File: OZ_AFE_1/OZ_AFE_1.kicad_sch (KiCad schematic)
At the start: 58 parts, among them U1 LT6011, U2 TLV2211, U3 ISL21009BFB825Z, U4 LT6011, U5 OGS, U6 MCP9700x-HTT

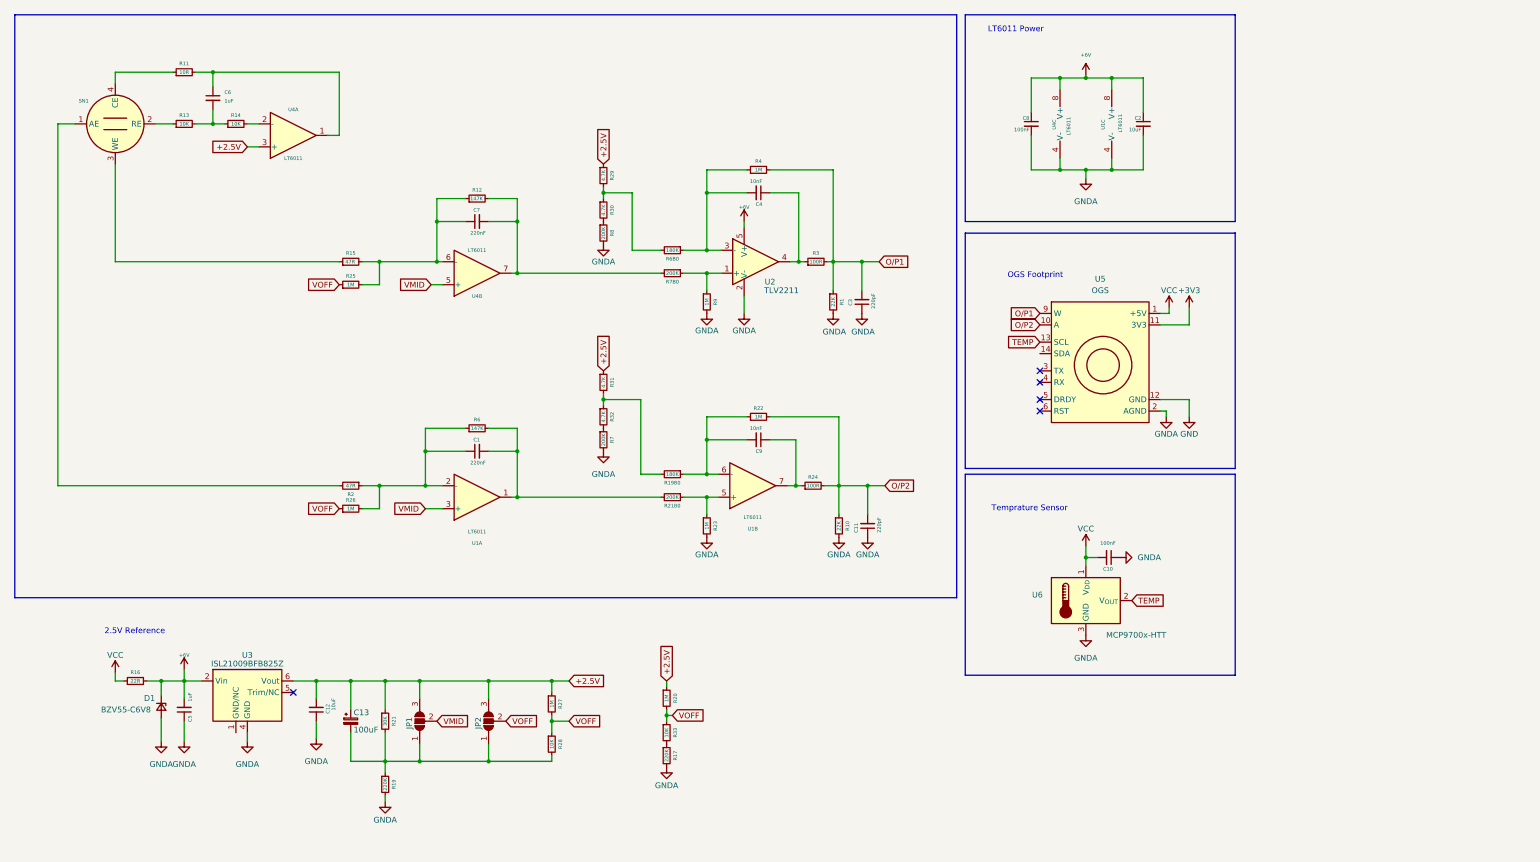
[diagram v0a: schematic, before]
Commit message: New Simulation and PCB
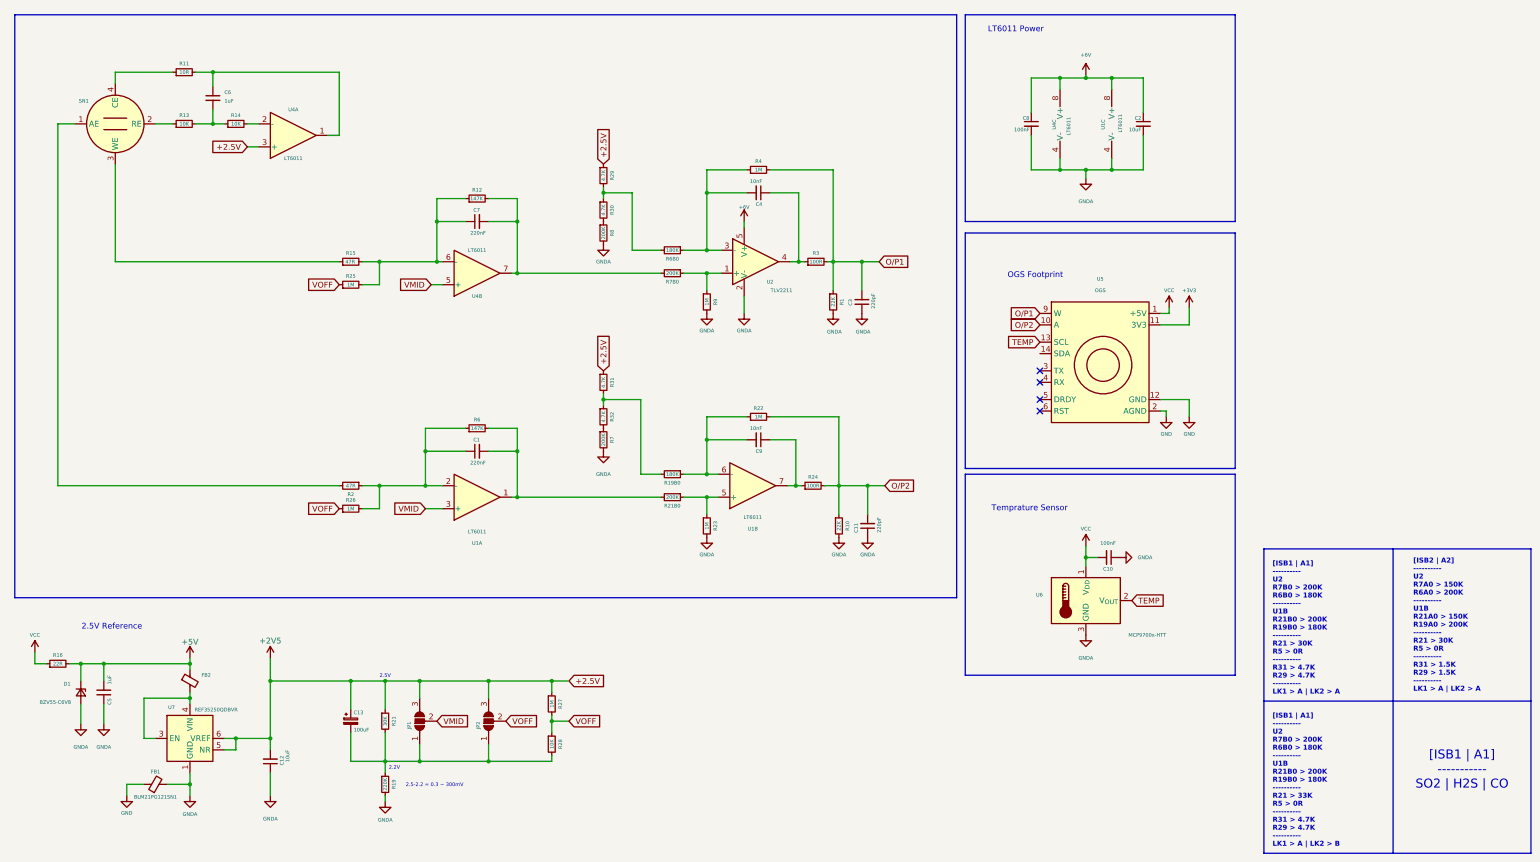
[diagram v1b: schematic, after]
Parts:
- removed R17: 220K, Resistor_SMD:R_0603_1608Metric, symbol Device:R_Small
- removed R20: 1M, Resistor_SMD:R_0603_1608Metric, symbol Device:R_Small
- removed R33: 10K, Resistor_SMD:R_0603_1608Metric, symbol Device:R_Small
- removed U3: ISL21009BFB825Z, Package_SO:SOIC-8_3.9x4.9mm_P1.27mm, symbol Voltage-Reference:ISL21009BFB825Z
- added FB1, FB2: BLM21PG121SN1, symbol Device:FerriteBead_Small
- added U7: REF35250QDBVR, Package_TO_SOT_SMD:SOT-23-6, symbol Reference_Voltage:REF35250QDBVR
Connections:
- net +6V: no longer C5.2, D1.1 (K), R16.2
- net GND: now also U5.2 (AGND), U5.8 (GND), FB1.1
- net GNDA: now also FB1.2, U7.1 (GND), U7.2 (GND); no longer U5.2 (AGND), U5.8 (GND)
- net +2.5V renamed +2V5
- net +2V5: now also U7.5 (NR), U7.6 (VREF)
- new net: FB2.2, U7.3 (EN), U7.4 (VIN)
- new net +5V: C5.2, D1.1 (K), FB2.1, R16.2
- no-connect marks 5 -> 4
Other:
- note added: "2.2V"
- note added: "2.5-2.2 = 0.3 ~ 300mV"
- note added: "2.5V"
- note added: "[ISB1 | A1] ---------- U2 R7B0 > 200K R6B0 > 180K ---------- U1B R21B0 > 200K R19B0 > 180K ---------- R21 > 30K R5 > 0R ---------- R31 > 4.7K R29 > 4.7K ---------- LK1 > A | LK2 > A"
- note added: "[ISB1 | A1] ---------- U2 R7B0 > 200K R6B0 > 180K ---------- U1B R21B0 > 200K R19B0 > 180K ---------- R21 > 33K R5 > 0R ---------- R31 > 4.7K R29 > 4.7K ---------- LK1 > A | LK2 > B"
- note added: "[ISB1 | A1] ----------- SO2 | H2S | CO"
- note added: "[ISB2 | A2] ---------- U2 R7A0 > 150K R6A0 > 200K ---------- U1B R21A0 > 150K R19A0 > 200K ---------- R21 > 30K R5 > 0R ---------- R31 > 1.5K R29 > 1.5K ---------- LK1 > A | LK2 > A"
- moved on the sheet: C12, C5, D1, R16

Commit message: update
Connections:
- net +5V: now also C2.1, C8.1, U1.8 (V+), U4.8 (V+)
- net +6V: no longer C2.1, C8.1, U1.8 (V+), U4.8 (V+)
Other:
- moved on the sheet: C1, C10, C11, C12, C13, C2, C3, C4, C5, C6, C7, C8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

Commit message: sch update
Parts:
- removed D1: BZV55-C6V8, Diode_SMD:D_MiniMELF, symbol Device:D_Zener_Small
- removed U2: TLV2211, Package_TO_SOT_SMD:SOT-23-5, symbol Operational-Amplifiers:TLV2211
- added C14: 100nF, Capacitor_SMD:C_0603_1608Metric, symbol Device:C_Small
- added C15: 1uF, Capacitor_SMD:C_0603_1608Metric, symbol Device:C_Small
- added C16, C17, C18, C19: 1nF, Capacitor_SMD:C_0402_1005Metric, symbol Device:C_Small
- added FB3, FB4, FB5, FB6: LQW18ANR47J00D, Inductor_SMD:L_0603_1608Metric, symbol Device:FerriteBead_Small
- added Q1, Q2: MMBFJ270, Package_TO_SOT_SMD:SOT-23, symbol Device:Q_PJFET_DSG
- added R17, R5: 1M, Resistor_SMD:R_0402_1005Metric, symbol Device:R_Small
- added U3: TLV8811, Package_TO_SOT_SMD:SOT-23-6, symbol TLV8811:TLV8811
- C2: value 10uF -> 100nF
- FB1, FB2: footprint (none) -> Resistor_SMD:R_0805_2012Metric
- JP1, JP2: footprint (none) -> Jumper:SolderJumper-3_P1.3mm_Open_RoundedPad1.0x1.5mm
- R1, R10, R13, R14, R15, R2, R22, R23, R24, R25, R26, R27, R28, R3, R4, R9: footprint Resistor_SMD:R_0603_1608Metric -> Resistor_SMD:R_0402_1005Metric
- U1, U4: value LT6011 -> LT6011IMS8#PBF; footprint Package_SO:SOIC-8_3.9x4.9mm_P1.27mm -> Package_SO:MSOP-8_3x3mm_P0.65mm
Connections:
- net +2V5: no longer U4.3 (+)
- net +5V: now also C14.1, R17.2, R5.2, U3.5 (V+)
- net GNDA: now also C14.2, C15.1, C16.2, C17.2, C18.2, C19.1, U3.2 (V-)
- net VMID: now also U1.5 (+); no longer U1.3 (+)
- net VOFF: no longer JP2.2 (C)
- net at C4.2, R4.1, R6B0.1: now also U4.2 (-)
- net at R21B0.1, R23.1: now also U1.3 (+); no longer U1.5 (+)
- net at C9.2, R19B0.1, R22.1: now also U1.2 (-); no longer U1.6 (-)
- net at C9.1, R24.1: now also U1.1; no longer U1.7
- net at R15.1: now also C17.1, FB3.2; no longer SN1.3 (WE)
- net at C4.1, R3.1: now also U4.1
- net at C1.1, R2.1, R26.2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: now also U1.6 (-); no longer U1.2 (-)
- net at R2.2: now also C16.1, FB4.2; no longer SN1.1 (AE)
- net at FB2.2, U7.3 (EN), U7.4 (VIN): now also C15.2
- net at C1.2, R21B0.2, R6.2: now also U1.7; no longer U1.1
- net at R11.1: now also C19.2, FB5.2; no longer SN1.4 (CE)
- net at C6.1, R11.2: now also U3.1; no longer U4.1
- net at R7B0.1, R9.1: now also U4.3 (+)
- net at R13.1: now also C18.1, FB6.2; no longer SN1.2 (RE)
- net at R14.2: now also U3.4 (-); no longer U4.2 (-)
- new net: Q1.3 (G), R5.1
- new net: FB5.1, SN1.4 (CE)
- new net: Q2.3 (G), R17.1
- new net AUX: FB4.1, Q2.2 (S), SN1.1 (AE)
- new net REF: FB6.1, Q1.1 (D), Q2.1 (D), SN1.2 (RE)
- new net VCE: JP2.2 (C), U3.3 (+)
- new net WORK: FB3.1, Q1.2 (S), SN1.3 (WE)
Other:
- moved on the sheet: C1, C11, C3, C4, C6, C7, C9, R1, R10, R11, R12, R13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
